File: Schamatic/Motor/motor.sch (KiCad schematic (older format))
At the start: 45 parts, among them J1 CONN_02X05, J11 V, J12 U, J13 W, J2 SPI, J3 RS485, J4 GND, J5 CAP+, J6 12, J7 GND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

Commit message: fixes to the boards
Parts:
- removed J5: CAP+, Pin_Headers:Pin_Header_Straight_1x01_Pitch2.54mm, symbol CONN_01X01
- removed J8: CAP-, Pin_Headers:Pin_Header_Straight_1x01_Pitch2.54mm, symbol CONN_01X01
- added D6: 47v, Diodes_SMD:D_SOD-123F, symbol D_Zener_Small
- C3: value 22uF -> 10uF; footprint Capacitors_SMD:C_0805 -> Capacitors_SMD:C_1206
- CALIB1: renamed from SW2; value SWiTCH -> CALIB
- D1, D4: footprint Diodes_SMD:D_0603 -> Diodes_SMD:D_SOD-323F
- ID1: renamed from SW1; value SWiTCH -> ID
- Y1: footprint Dizzy:OSC_CSTCE16M0V53-R0 -> Dizzy:Oscillator
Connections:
- net CS: now also J2.2 (P2); no longer J2.4 (P4)
- net Earth: now also J2.1 (P1), D6.2 (A); no longer J2.5 (P5)
- net MISO: now also J2.5 (P5); no longer J2.2 (P2)
- net MOSI: now also J2.4 (P4); no longer J2.1 (P1)
- net VM: now also D6.1 (K)

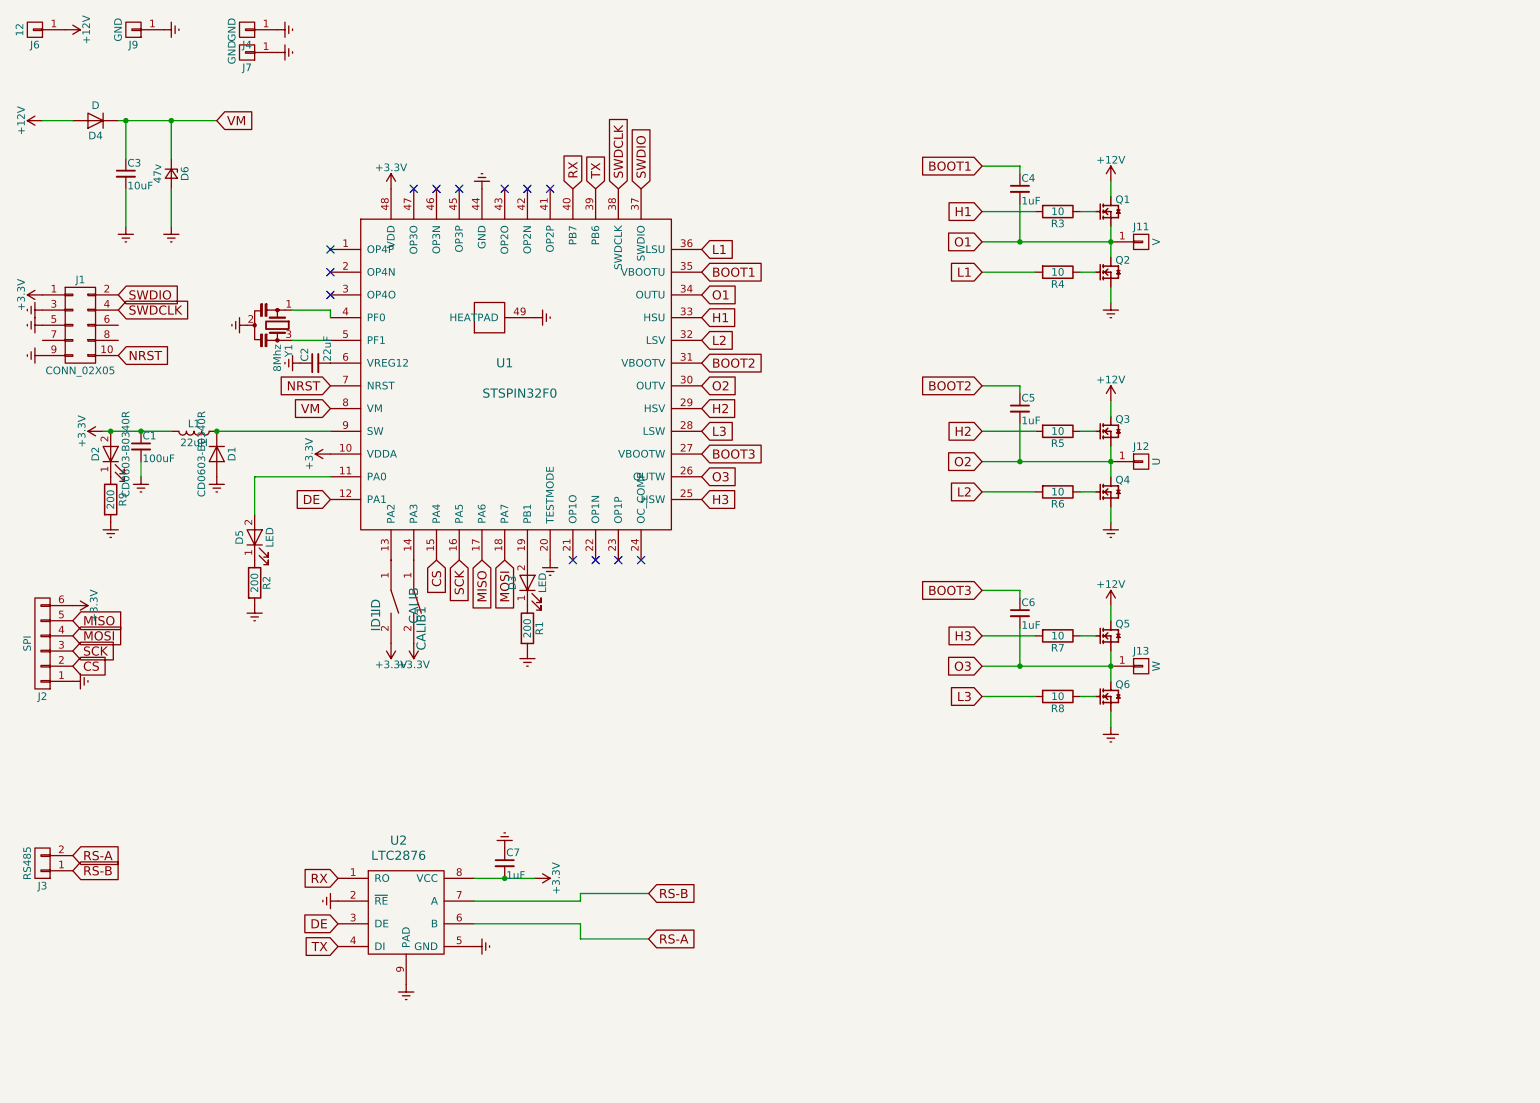
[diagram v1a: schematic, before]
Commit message: external motor controller
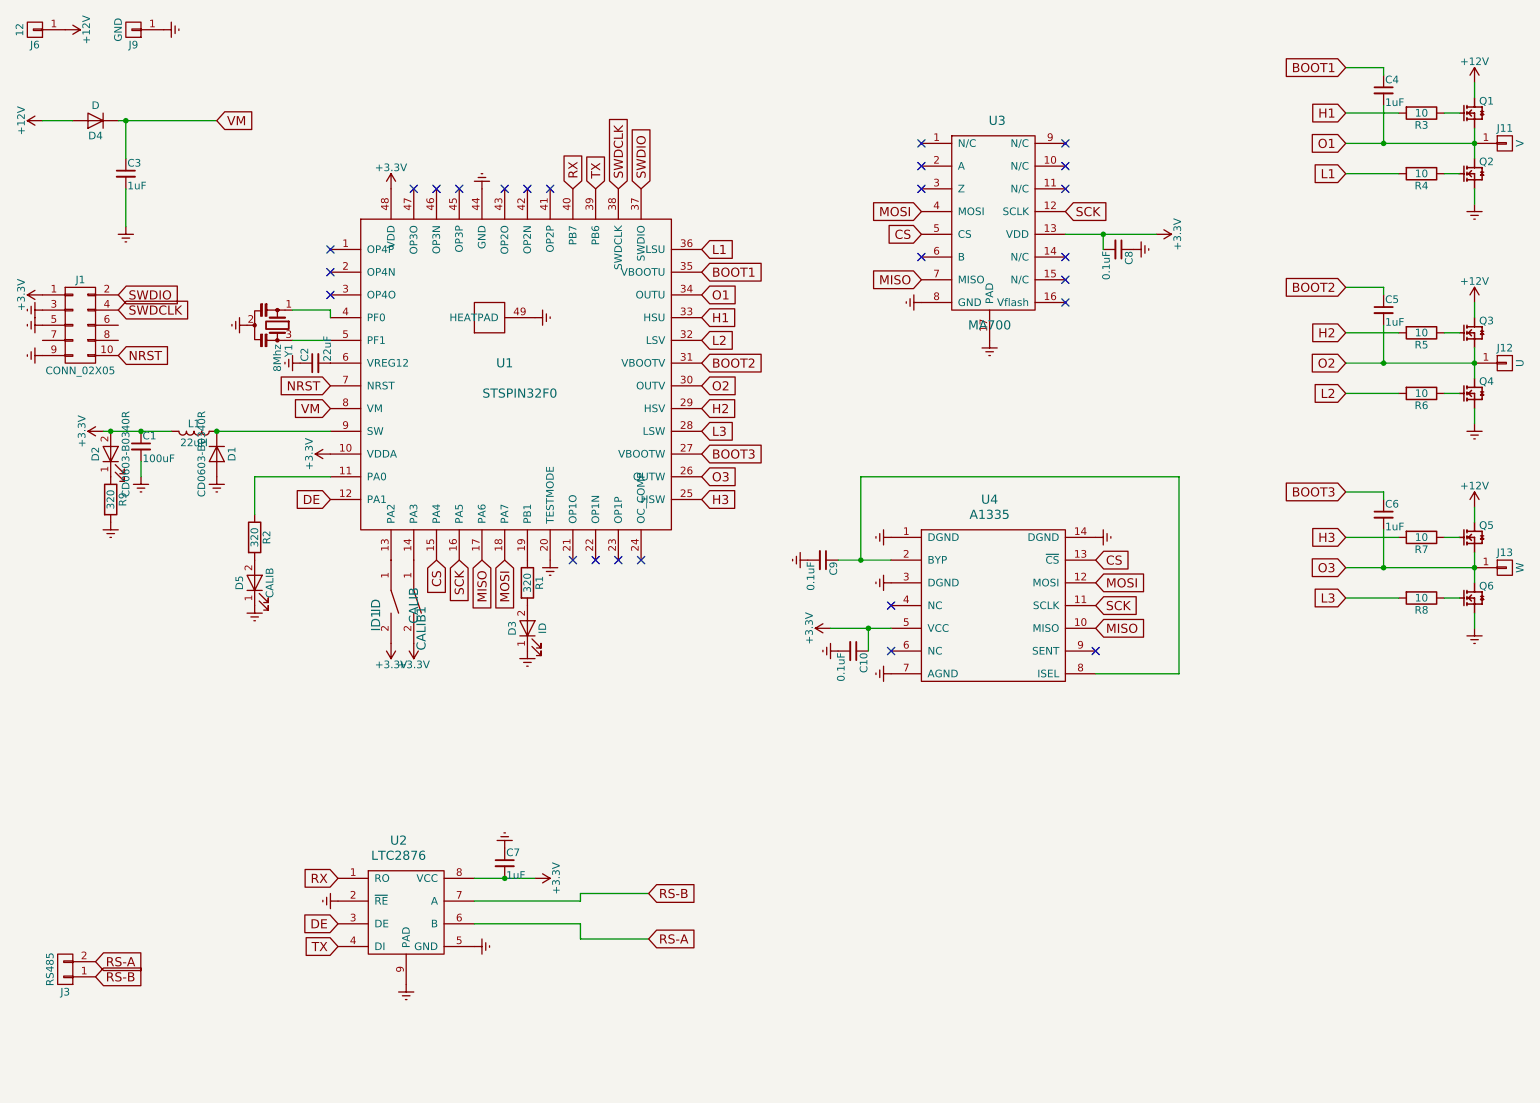
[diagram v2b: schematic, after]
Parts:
- removed D6: 47v, Diodes_SMD:D_SOD-123F, symbol D_Zener_Small
- removed J2: SPI, Dizzy:SPI_CONN, symbol CONN_01X06
- removed J4, J7: GND, Pin_Headers:Pin_Header_Straight_1x01_Pitch2.54mm, symbol CONN_01X01
- added C10, C8, C9: 0.1uF, Capacitors_SMD:C_0603, symbol C_Small
- added U3: MA700, Housings_DFN_QFN:QFN-16-1EP_3x3mm_Pitch0.5mm, symbol MA700
- added U4: A1335, Housings_SSOP:TSSOP-14_4.4x5mm_Pitch0.65mm, symbol A1335
- C3: value 10uF -> 1uF
- D3: value LED -> ID
- D5: value LED -> CALIB
- J1: footprint Pin_Headers:Pin_Header_Straight_2x05_Pitch1.27mm -> Pin_Headers:Pin_Header_Straight_2x05_Pitch1.27mm_SMD
- Q2, Q4, Q6: footprint Dizzy:PSMN3R3-40YS -> Dizzy:PSMN3R3-40YS-vias
- R1, R2, R9: value 200 -> 320
- U1: footprint Dizzy:STSPIN32F0 -> Dizzy:STSPIN32-nopad
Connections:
- net +3V3: now also C10.1, C8.2, U3.13 (VDD), U4.5 (VCC)
- net CS: now also U3.5 (CS), U4.13 (~CS)
- net Earth: now also D3.1 (K), D5.1 (K), C10.2, C8.1, C9.2, U3.17 (PAD), U3.8 (GND), U4.1 (DGND), U4.14 (DGND), U4.3 (DGND), U4.7 (AGND); no longer R1.2, R2.2
- net MISO: now also U3.7 (MISO), U4.10 (MISO)
- net MOSI: now also U3.4 (MOSI), U4.12 (MOSI)
- net SCK: now also U3.12 (SCLK), U4.11 (SCLK)
- net at D5.2 (A): now also R2.2; no longer U1.11 (PA0)
- net at D3.2 (A): now also R1.2; no longer U1.19 (PB1)
- net at R1.1: now also U1.19 (PB1); no longer D3.1 (K)
- net at R2.1: now also U1.11 (PA0); no longer D5.1 (K)
- new net: C9.1, U4.2 (BYP), U4.8 (ISEL)
- no-connect marks 13 -> 26
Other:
- moved on the sheet: C4, C5, C6, D3, D5, J11, J12, J13, J3, Q1, Q2, Q3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

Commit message: high voltage controller
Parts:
- removed U4: A1335, Housings_SSOP:TSSOP-14_4.4x5mm_Pitch0.65mm, symbol A1335
- added C11: 4.7uF, Capacitors_SMD:C_1206, symbol C_Small
- added C12: 0.1uF, Capacitors_SMD:C_0603, symbol C_Small
- added L2: 220uH, Inductors_SMD:L_1210, symbol L_Small
- added R10: 237K, Capacitors_SMD:C_0603, symbol R_Small
- added R11, R13: 10K, Capacitors_SMD:C_0603, symbol R_Small
- added R12: 230K, Capacitors_SMD:C_0603, symbol R_Small
- added R14: 1Ohm, Capacitors_SMD:C_0603, symbol R_Small
- added U4: LM5019, Housings_DFN_QFN:DFN-8-1EP_4x4mm_Pitch0.8mm, symbol LM5019
- C1: footprint Capacitors_SMD:C_0805 -> Capacitors_SMD:C_1210
- C10: value 0.1uF -> 0.01uF
- C3: value 1uF -> 2uF; footprint Capacitors_SMD:C_1206 -> Capacitors_SMD:C_1210
- C9: value 0.1uF -> 1uF
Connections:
- net +3V3: now also C12.2, R11.1; no longer C10.1
- net DE: now also U2.2 (~RE)
- net Earth: now also C11.2, C12.1, R13.2, U4.1 (RTN), U4.9 (PAD); no longer C10.2, U2.2 (~RE)
- net NRST: now also R11.2
- net VM: now also L2.2, R12.1, R14.1; no longer C3.1, D4.1 (K)
- net at C9.1: now also U4.6 (VCC)
- new net: C3.1, D4.1 (K), R10.2, U4.2 (VIN), U4.3 (UVLO)
- new net: R10.1, U4.4 (RON)
- new net: R12.2, R13.1, U4.5 (FB)
- new net: C10.1, U4.7 (BST)
- new net: C10.2, L2.1, U4.8 (SW)
- new net: C11.1, R14.2
- no-connect marks 26 -> 23
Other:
- moved on the sheet: C3, C7, D4, J1, J6, J9, U2

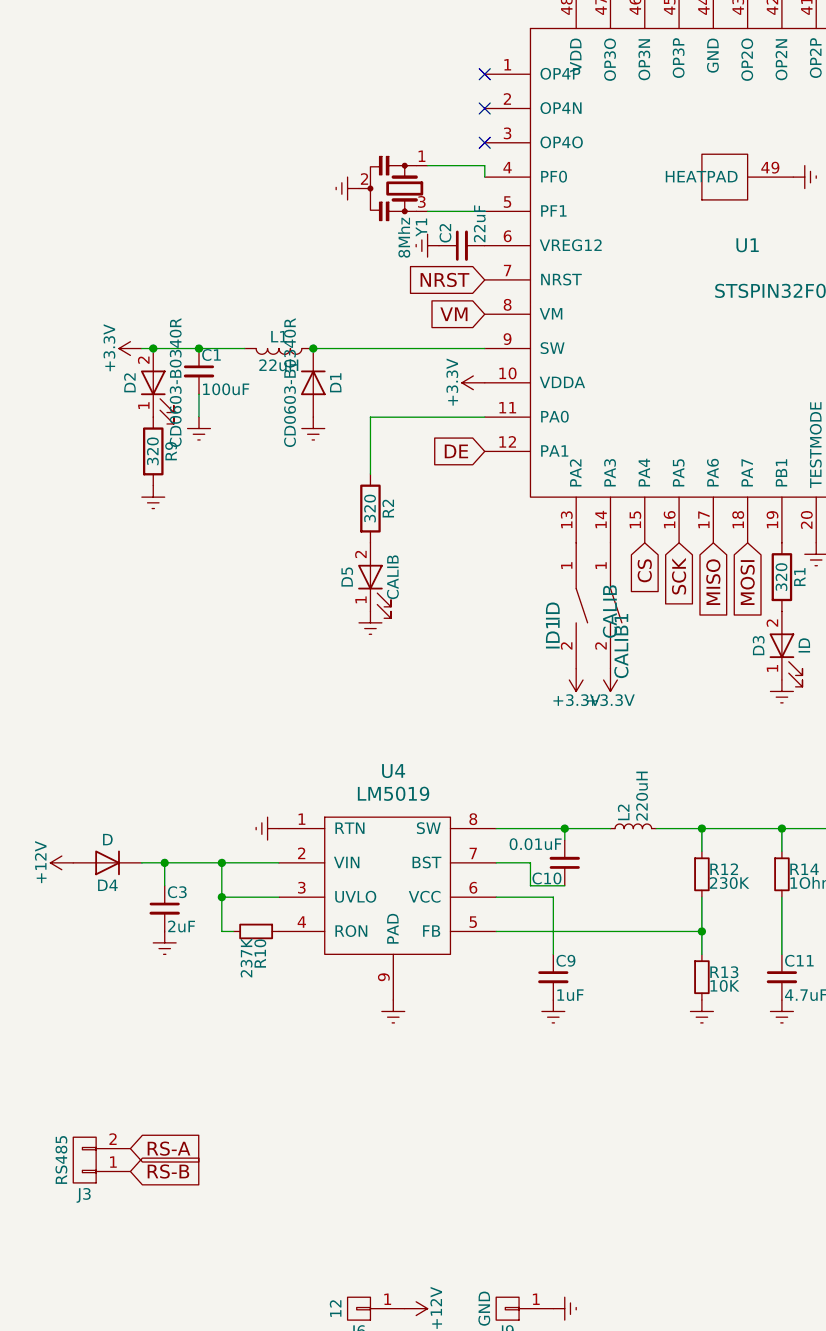
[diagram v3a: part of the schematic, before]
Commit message: this was failed attempt to increase voltage
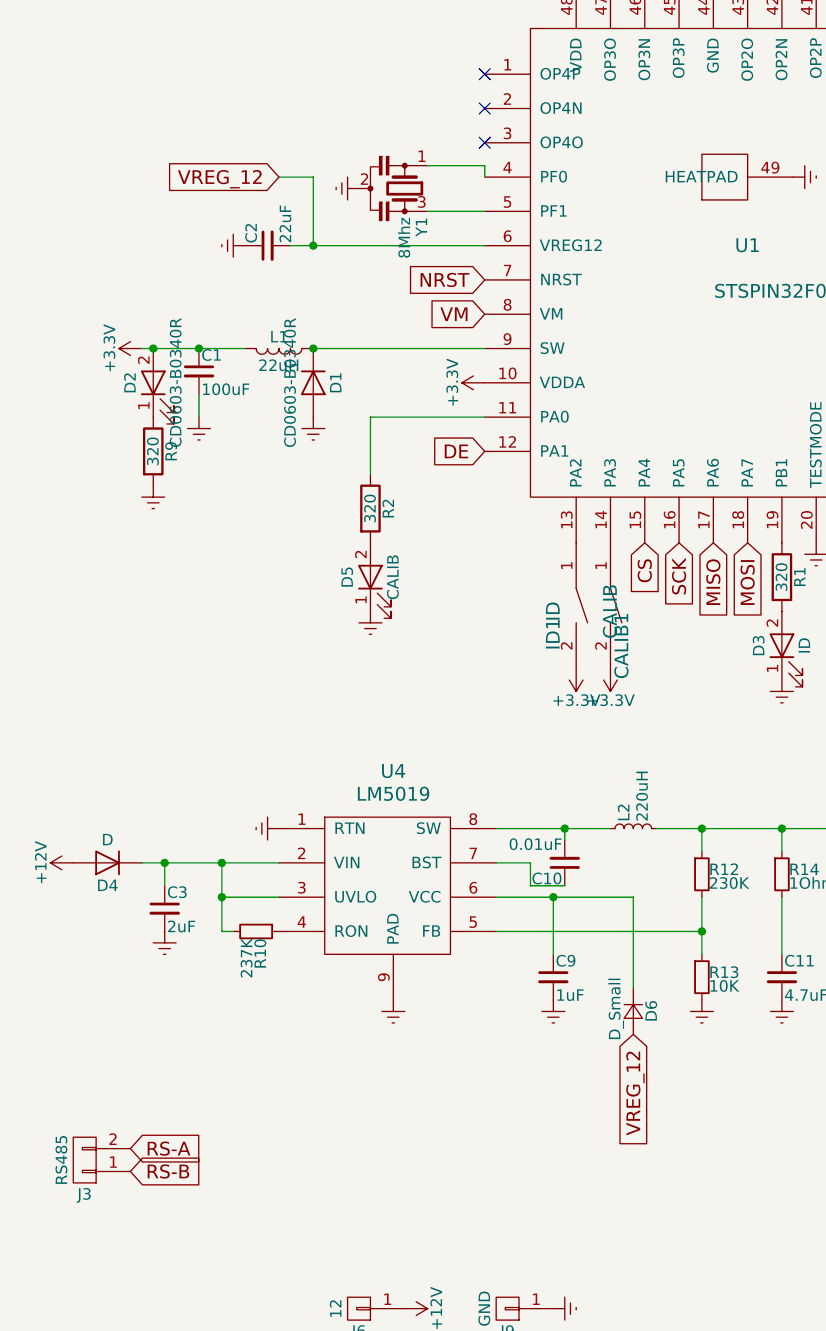
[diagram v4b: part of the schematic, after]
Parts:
- added D6: D_Small, Diodes_SMD:D_SOD-323F, symbol D_Small
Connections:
- net VREG_12: now reaches C2.2, U1.6 (VREG12)
- net VREG_12: now also D6.2 (A)
- net at C9.1, U4.6 (VCC): now also D6.1 (K)
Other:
- moved on the sheet: C2
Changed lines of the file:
@@
 L Earth #PWR012
 U 1 1 59781423
-P 2450 2900
-F 0 "#PWR012" H 2450 2650 50  0001 C CNN
-F 1 "Earth" H 2450 2750 50  0001 C CNN
-F 2 "" H 2450 2900 50  0001 C CNN
-F 3 "" H 2450 2900 50  0001 C CNN
-	1    2450 2900
+P 1600 2900
+F 0 "#PWR012" H 1600 2650 50  0001 C CNN
+F 1 "Earth" H 1600 2750 50  0001 C CNN
+F 2 "" H 1600 2900 50  0001 C CNN
+F 3 "" H 1600 2900 50  0001 C CNN
+	1    1600 2900
 	0    1    1    0
 $EndComp
@@
 L C_Small C2
 U 1 1 59C72B99
-P 2550 2900
-F 0 "C2" H 2560 2970 50  0000 L CNN
-F 1 "22uF" H 2560 2820 50  0000 L CNN
-F 2 "Capacitors_SMD:C_0805" H 2550 2900 50  0001 C CNN
-F 3 "" H 2550 2900 50  0001 C CNN
-	1    2550 2900
+P 1700 2900
+F 0 "C2" H 1710 2970 50  0000 L CNN
+F 1 "22uF" H 1710 2820 50  0000 L CNN
+F 2 "Capacitors_SMD:C_0805" H 1700 2900 50  0001 C CNN
+F 3 "" H 1700 2900 50  0001 C CNN
+	1    1700 2900
 	0    -1   -1   0
 $EndComp
@@
 $EndComp
 $Comp
-L Earth #PWR027
+L Earth #PWR026
 U 1 1 59CACEFE
 P 1200 3950
-F 0 "#PWR027" H 1200 3700 50  0001 C CNN
+F 0 "#PWR026" H 1200 3700 50  0001 C CNN
 F 1 "Earth" H 1200 3800 50  0001 C CNN
 F 2 "" H 1200 3950 50  0001 C CNN
@@
 $EndComp
 $Comp
-L +12V #PWR028
+L +12V #PWR027
 U 1 1 59CA4ECB
 P 2300 7550
-F 0 "#PWR028" H 2300 7400 50  0001 C CNN
+F 0 "#PWR027" H 2300 7400 50  0001 C CNN
 F 1 "+12V" H 2300 7690 50  0000 C CNN
 F 2 "" H 2300 7550 50  0001 C CNN
@@
 $EndComp
 $Comp
-L Earth #PWR029
+L Earth #PWR028
 U 1 1 5A06D2CF
 P 2150 4500
-F 0 "#PWR029" H 2150 4250 50  0001 C CNN
+F 0 "#PWR028" H 2150 4250 50  0001 C CNN
 F 1 "Earth" H 2150 4350 50  0001 C CNN
 F 2 "" H 2150 4500 50  0001 C CNN
@@
 $EndComp
 $Comp
-L Earth #PWR030
+L Earth #PWR029
 U 1 1 5A0724EC
 P 1250 5900
-F 0 "#PWR030" H 1250 5650 50  0001 C CNN
+F 0 "#PWR029" H 1250 5650 50  0001 C CNN
 F 1 "Earth" H 1250 5750 50  0001 C CNN
 F 2 "" H 1250 5900 50  0001 C CNN
@@
 $EndComp
 $Comp
-L Earth #PWR031
+L Earth #PWR030
 U 1 1 5A06E0D7
 P 6100 5950
-F 0 "#PWR031" H 6100 5700 50  0001 C CNN
+F 0 "#PWR030" H 6100 5700 50  0001 C CNN
 F 1 "Earth" H 6100 5800 50  0001 C CNN
 F 2 "" H 6100 5950 50  0001 C CNN
@@
 $EndComp
 $Comp
-L Earth #PWR032
+L Earth #PWR031
 U 1 1 5A621AD5
 P 800 1350
-F 0 "#PWR032" H 800 1100 50  0001 C CNN
+F 0 "#PWR031" H 800 1100 50  0001 C CNN
 F 1 "Earth" H 800 1200 50  0001 C CNN
 F 2 "" H 800 1350 50  0001 C CNN
@@
 $EndComp
 $Comp
-L Earth #PWR033
+L Earth #PWR032
 U 1 1 5A621D43
 P 800 1450
-F 0 "#PWR033" H 800 1200 50  0001 C CNN
+F 0 "#PWR032" H 800 1200 50  0001 C CNN
 F 1 "Earth" H 800 1300 50  0001 C CNN
 F 2 "" H 800 1450 50  0001 C CNN
@@
 $EndComp
 $Comp
-L Earth #PWR034
+L Earth #PWR033
 U 1 1 5A622EE0
 P 800 1650
-F 0 "#PWR034" H 800 1400 50  0001 C CNN
+F 0 "#PWR033" H 800 1400 50  0001 C CNN
 F 1 "Earth" H 800 1500 50  0001 C CNN
 F 2 "" H 800 1650 50  0001 C CNN
@@
 $EndComp
 $Comp
-L Earth #PWR035
+L Earth #PWR034
 U 1 1 5ADF0D23
 P 6550 2500
-F 0 "#PWR035" H 6550 2250 50  0001 C CNN
+F 0 "#PWR034" H 6550 2250 50  0001 C CNN
 F 1 "Earth" H 6550 2350 50  0001 C CNN
 F 2 "" H 6550 2500 50  0001 C CNN
@@
 NoConn ~ 7500 2500
 $Comp
-L Earth #PWR036
+L Earth #PWR035
 U 1 1 59CA5287
 P 2950 7550
-F 0 "#PWR036" H 2950 7300 50  0001 C CNN
+F 0 "#PWR035" H 2950 7300 50  0001 C CNN
 F 1 "Earth" H 2950 7400 50  0001 C CNN
 F 2 "" H 2950 7550 50  0001 C CNN
@@
 Connection ~ 7750 2050
 $Comp
-L Earth #PWR037
+L Earth #PWR036
 U 1 1 5ADFAAAA
 P 7950 2150
-F 0 "#PWR037" H 7950 1900 50  0001 C CNN
+F 0 "#PWR036" H 7950 1900 50  0001 C CNN
 F 1 "Earth" H 7950 2000 50  0001 C CNN
 F 2 "" H 7950 2150 50  0001 C CNN
@@
 $EndComp
 $Comp
-L Earth #PWR038
+L Earth #PWR037
 U 1 1 5AE3079B
 P 7000 2750
-F 0 "#PWR038" H 7000 2500 50  0001 C CNN
+F 0 "#PWR037" H 7000 2500 50  0001 C CNN
 F 1 "Earth" H 7000 2600 50  0001 C CNN
 F 2 "" H 7000 2750 50  0001 C CNN
@@
 Connection ~ 1500 5750
 $Comp
-L Earth #PWR039
+L Earth #PWR038
 U 1 1 5B0D5395
 P 2250 6200
-F 0 "#PWR039" H 2250 5950 50  0001 C CNN
+F 0 "#PWR038" H 2250 5950 50  0001 C CNN
 F 1 "Earth" H 2250 6050 50  0001 C CNN
 F 2 "" H 2250 6200 50  0001 C CNN
@@
 $EndComp
 $Comp
-L Earth #PWR040
+L Earth #PWR039
 U 1 1 5B0D5424
 P 1750 5450
-F 0 "#PWR040" H 1750 5200 50  0001 C CNN
+F 0 "#PWR039" H 1750 5200 50  0001 C CNN
 F 1 "Earth" H 1750 5300 50  0001 C CNN
 F 2 "" H 1750 5450 50  0001 C CNN
@@
 	2850 5600 2700 5600
 Wire Wire Line
-	2700 5750 2950 5750
+	2700 5750 3300 5750
 Wire Wire Line
 	2950 5750 2950 6000
 $Comp
-L Earth #PWR041
+L Earth #PWR040
 U 1 1 5B0D5DD7
 P 2950 6200
-F 0 "#PWR041" H 2950 5950 50  0001 C CNN
+F 0 "#PWR040" H 2950 5950 50  0001 C CNN
 F 1 "Earth" H 2950 6050 50  0001 C CNN
 F 2 "" H 2950 6200 50  0001 C CNN
@@
 	3950 6000 3950 5750
 $Comp
-L Earth #PWR042
+L Earth #PWR041
 U 1 1 5B0D638A
 P 3600 6200
-F 0 "#PWR042" H 3600 5950 50  0001 C CNN
+F 0 "#PWR041" H 3600 5950 50  0001 C CNN
 F 1 "Earth" H 3600 6050 50  0001 C CNN
 F 2 "" H 3600 6200 50  0001 C CNN
@@
 $EndComp
 $Comp
-L Earth #PWR043
+L Earth #PWR042
 U 1 1 5B0D642E
 P 3950 6200
-F 0 "#PWR043" H 3950 5950 50  0001 C CNN
+F 0 "#PWR042" H 3950 5950 50  0001 C CNN
 F 1 "Earth" H 3950 6050 50  0001 C CNN
 F 2 "" H 3950 6200 50  0001 C CNN
@@
 	1300 1650 2000 1650
 $Comp
-L +3.3V #PWR044
+L +3.3V #PWR043
 U 1 1 5B0DB1DB
 P 1850 1300
-F 0 "#PWR044" H 1850 1150 50  0001 C CNN
+F 0 "#PWR043" H 1850 1150 50  0001 C CNN
 F 1 "+3.3V" H 1850 1440 50  0000 C CNN
 F 2 "" H 1850 1300 50  0001 C CNN
@@
 	3050 1750 3050 1450
 $Comp
-L Earth #PWR045
+L Earth #PWR044
 U 1 1 5B0E1AE7
 P 2850 1450
-F 0 "#PWR045" H 2850 1200 50  0001 C CNN
+F 0 "#PWR044" H 2850 1200 50  0001 C CNN
 F 1 "Earth" H 2850 1300 50  0001 C CNN
 F 2 "" H 2850 1450 50  0001 C CNN
@@
 	5650 5400 5650 5550
 Connection ~ 5650 5550
+Wire Wire Line
+	1800 2900 2650 2900
+Text GLabel 1750 2600 0    60   Input ~ 0
+VREG_12
+Wire Wire Line
+	1750 2600 1900 2600
+Wire Wire Line
+	1900 2600 1900 2900
+Connection ~ 1900 2900
+Text GLabel 3300 6350 3    60   Input ~ 0
+VREG_12
+$Comp
+L D_Small D6
+U 1 1 5B0FDBD1
+P 3300 6250
+F 0 "D6" H 3250 6330 50  0000 L CNN
+F 1 "D_Small" H 3150 6170 50  0000 L CNN
+F 2 "Diodes_SMD:D_SOD-323F" V 3300 6250 50  0001 C CNN
+F 3 "" V 3300 6250 50  0001 C CNN
+	1    3300 6250
+	0    1    1    0
+$EndComp
+Wire Wire Line
+	3300 5750 3300 6150
+Connection ~ 2950 5750
 $EndSCHEMATC
